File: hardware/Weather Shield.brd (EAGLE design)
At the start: 53.3 x 59.7 mm, 46 parts, among them Q1 BSS138, Q2 BSS138, U1 ARDUINO_R3_SHIELD, U2 3.3V MIC5219, U4 MPL3115A2LGA8, U5 HTU21D, U7 GP-635T, U8 TEMT6000

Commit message: Added power ctl to GPS and backup battery connection.
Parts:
- added JP1: Ext Batt, SparkFun-Connectors:1X01
- added LOGO1: OSHW-LOGOM, SparkFun-Aesthetics:OSHW-LOGO-M
- added R9: 1K, SparkFun:0603-RES
- moved FRAME1 63.6 mm to (-8.89, -24.1)
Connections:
- new net 3V_PWR_CTL: R9.2, U7.1
- net PWR_CTL: now also R9.1; no longer U7.1
- net V_BATT: now also JP1.1
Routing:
- net V_BATT: track 0.00 -> 12.2 mm, vias 0 -> 1
- net PWR_CTL: track 90.8 -> 79.8 mm
- net 3V_PWR_CTL: track 0.00 -> 9.31 mm
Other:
- board text added: "Ext Batt"
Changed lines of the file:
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@@
 <layer number="39" name="tKeepout" color="4" fill="11" visible="no" active="yes"/>
 <layer number="40" name="bKeepout" color="1" fill="11" visible="no" active="yes"/>
-<layer number="41" name="tRestrict" color="4" fill="10" visible="yes" active="yes"/>
-<layer number="42" name="bRestrict" color="1" fill="10" visible="yes" active="yes"/>
+<layer number="41" name="tRestrict" color="4" fill="10" visible="no" active="yes"/>
+<layer number="42" name="bRestrict" color="1" fill="10" visible="no" active="yes"/>
 <layer number="43" name="vRestrict" color="2" fill="10" visible="no" active="yes"/>
 <layer number="44" name="Drills" color="7" fill="1" visible="no" active="yes"/>
@@
 <wire x1="0" y1="57.15" x2="0" y2="2.54" width="0.2032" layer="20"/>
 <text x="17.907" y="1.27" size="1.524" layer="21" ratio="15">Weather Shield</text>
-<text x="-60.96" y="-33.02" size="1.778" layer="21" font="vector" ratio="15">N. Seidle</text>
+<text x="22.86" y="-24.13" size="1.778" layer="21" font="vector" ratio="15">N. Seidle</text>
 <text x="22.225" y="24.257" size="1.27" layer="21" ratio="15">Pressure</text>
 <text x="14.986" y="33.655" size="1.27" layer="21" ratio="15">Humidity</text>
@@
 <rectangle x1="13.97" y1="24.13" x2="40.64" y2="36.83" layer="41"/>
 <rectangle x1="13.97" y1="24.13" x2="40.64" y2="36.83" layer="42"/>
+<text x="32.004" y="13.462" size="1.27" layer="21" ratio="15">Ext Batt</text>
 </plain>
 <attributes>
@@
 <element name="C14" library="SparkFun-Passives" package="EIA3216" value="10uF" x="21.59" y="19.05" rot="R90"/>
 <element name="U1" library="SparkFun-Boards" package="UNO_R3_SHIELD" value="ARDUINO_R3_SHIELD" x="0" y="0"/>
-<element name="FRAME1" library="SparkFun-Aesthetics" package="CREATIVE_COMMONS" value="FRAME-LETTER" x="-72.39" y="-26.67"/>
+<element name="FRAME1" library="SparkFun-Aesthetics" package="CREATIVE_COMMONS" value="FRAME-LETTER" x="-8.89" y="-24.13"/>
 <element name="Q1" library="SparkFun" package="SOT23-3" value="BSS138" x="43.18" y="27.94"/>
 <element name="R3" library="SparkFun" package="0603-RES" value="4.7K" x="43.18" y="24.13"/>
@@
 <element name="R7" library="SparkFun" package="0603-RES" value="1K" x="40.64" y="20.32" rot="R90"/>
 <element name="R8" library="SparkFun" package="0603-RES" value="3.9K" x="38.1" y="20.32" rot="R270"/>
+<element name="LOGO1" library="SparkFun-Aesthetics" package="OSHW-LOGO-M" value="OSHW-LOGOM" x="26.67" y="43.18"/>
+<element name="R9" library="SparkFun" package="0603-RES" value="1K" x="41.91" y="11.43"/>
+<element name="JP1" library="SparkFun-Connectors" package="1X01" value="Ext Batt" x="41.91" y="13.97"/>
 </elements>
 <signals>
@@
 <signal name="V_BATT">
 <contactref element="U7" pad="2"/>
+<contactref element="JP1" pad="1"/>
+<wire x1="52.07" y1="10.43" x2="44.72" y2="10.43" width="0.254" layer="1"/>
+<wire x1="44.72" y1="10.43" x2="44.45" y2="10.414" width="0.254" layer="1"/>
+<via x="44.45" y="10.414" extent="1-16" drill="0.508"/>
+<wire x1="41.91" y1="13.97" x2="41.91" y2="12.954" width="0.254" layer="16"/>
+<wire x1="41.91" y1="12.954" x2="44.45" y2="10.414" width="0.254" layer="16"/>
 </signal>
 <signal name="LIGHT">
@@
 </signal>
 <signal name="PWR_CTL">
-<contactref element="U7" pad="1"/>
 <contactref element="U1" pad="D6"/>
-<wire x1="52.07" y1="11.43" x2="30.48" y2="11.43" width="0.254" layer="1"/>
 <wire x1="2.54" y1="39.37" x2="3.81" y2="39.37" width="0.254" layer="16"/>
 <wire x1="3.81" y1="39.37" x2="5.08" y2="38.1" width="0.254" layer="16"/>
@@
 <wire x1="17.78" y1="11.43" x2="30.48" y2="11.43" width="0.254" layer="16"/>
 <via x="30.48" y="11.43" extent="1-16" drill="0.508"/>
+<contactref element="R9" pad="1"/>
+<wire x1="41.06" y1="11.43" x2="30.48" y2="11.43" width="0.254" layer="1"/>
 </signal>
 <signal name="GTXO">
@@
 <wire x1="39.37" y1="19.47" x2="38.1" y2="19.47" width="0.254" layer="1"/>
 </signal>
+<signal name="3V_PWR_CTL">
+<contactref element="U7" pad="1"/>
+<contactref element="R9" pad="2"/>
+<wire x1="42.76" y1="11.43" x2="52.07" y2="11.43" width="0.254" layer="1"/>
+</signal>
 </signals>

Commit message: Tweaked schematic labels and connector for backup battery.
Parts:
- removed JP1: Ext Batt, SparkFun-Connectors:1X01
- added JP2: M02PTH, SparkFun-Connectors:1X02
- R9: value 1K -> 4.7K
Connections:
- net GND: now also JP2.1
- net V_BATT: now also JP2.2; no longer JP1.1
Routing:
- net V_BATT: track 12.2 -> 11.2 mm
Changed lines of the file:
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@@
 <element name="R8" library="SparkFun" package="0603-RES" value="3.9K" x="38.1" y="20.32" rot="R270"/>
 <element name="LOGO1" library="SparkFun-Aesthetics" package="OSHW-LOGO-M" value="OSHW-LOGOM" x="26.67" y="43.18"/>
-<element name="R9" library="SparkFun" package="0603-RES" value="1K" x="41.91" y="11.43"/>
-<element name="JP1" library="SparkFun-Connectors" package="1X01" value="Ext Batt" x="41.91" y="13.97"/>
+<element name="R9" library="SparkFun" package="0603-RES" value="4.7K" x="41.91" y="11.43"/>
+<element name="JP2" library="SparkFun-Connectors" package="1X02" value="M02PTH" x="44.45" y="13.97" rot="R180"/>
 </elements>
 <signals>
@@
 <wire x1="27.94" y1="25.4" x2="31.33" y2="25.4" width="0.254" layer="1"/>
 <wire x1="31.33" y1="26.67" x2="33.44" y2="26.67" width="0.254" layer="1"/>
+<contactref element="JP2" pad="1"/>
 </signal>
 <signal name="STAT2">
@@
 <signal name="V_BATT">
 <contactref element="U7" pad="2"/>
-<contactref element="JP1" pad="1"/>
 <wire x1="52.07" y1="10.43" x2="44.72" y2="10.43" width="0.254" layer="1"/>
 <wire x1="44.72" y1="10.43" x2="44.45" y2="10.414" width="0.254" layer="1"/>
 <via x="44.45" y="10.414" extent="1-16" drill="0.508"/>
-<wire x1="41.91" y1="13.97" x2="41.91" y2="12.954" width="0.254" layer="16"/>
 <wire x1="41.91" y1="12.954" x2="44.45" y2="10.414" width="0.254" layer="16"/>
+<contactref element="JP2" pad="2"/>
+<wire x1="41.91" y1="13.97" x2="41.91" y2="12.954" width="0" layer="19" extent="16-16"/>
 </signal>
 <signal name="LIGHT">

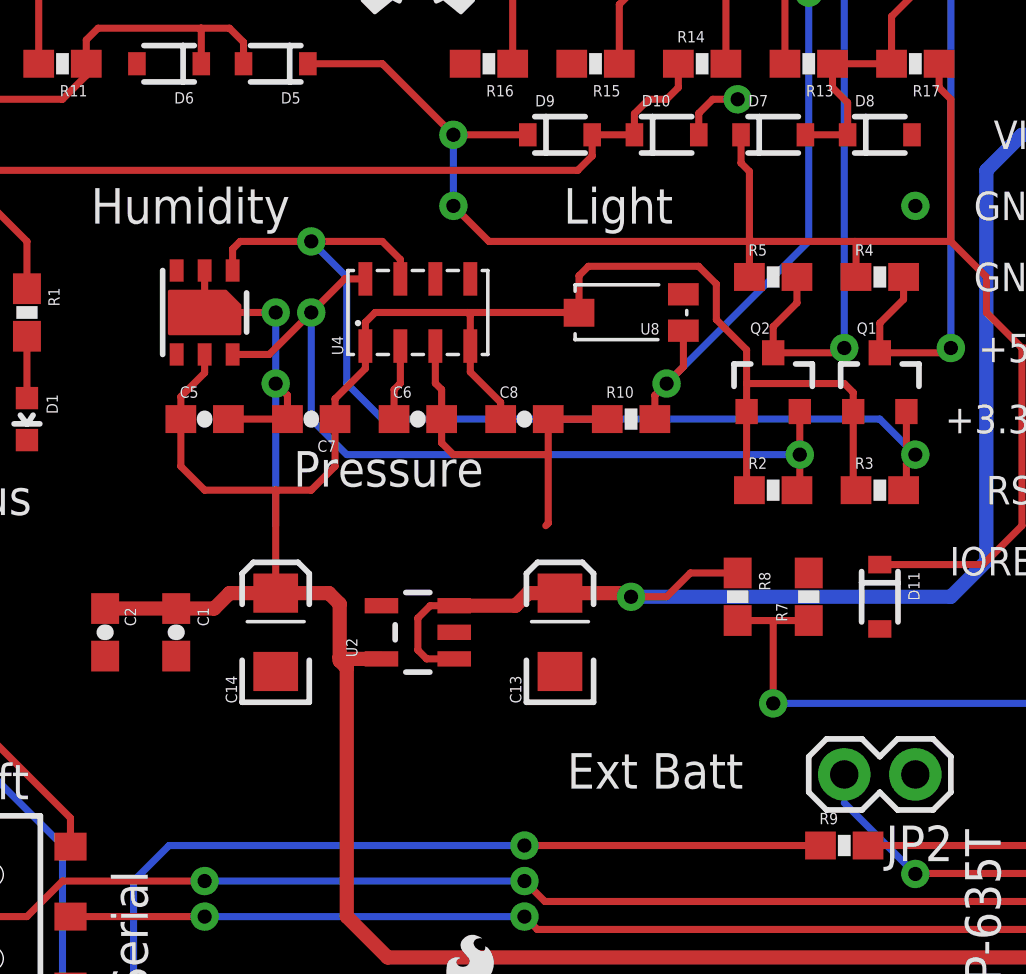
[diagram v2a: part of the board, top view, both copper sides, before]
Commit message: Added support for smaller, cheaper ALS-PT19 light sensor.
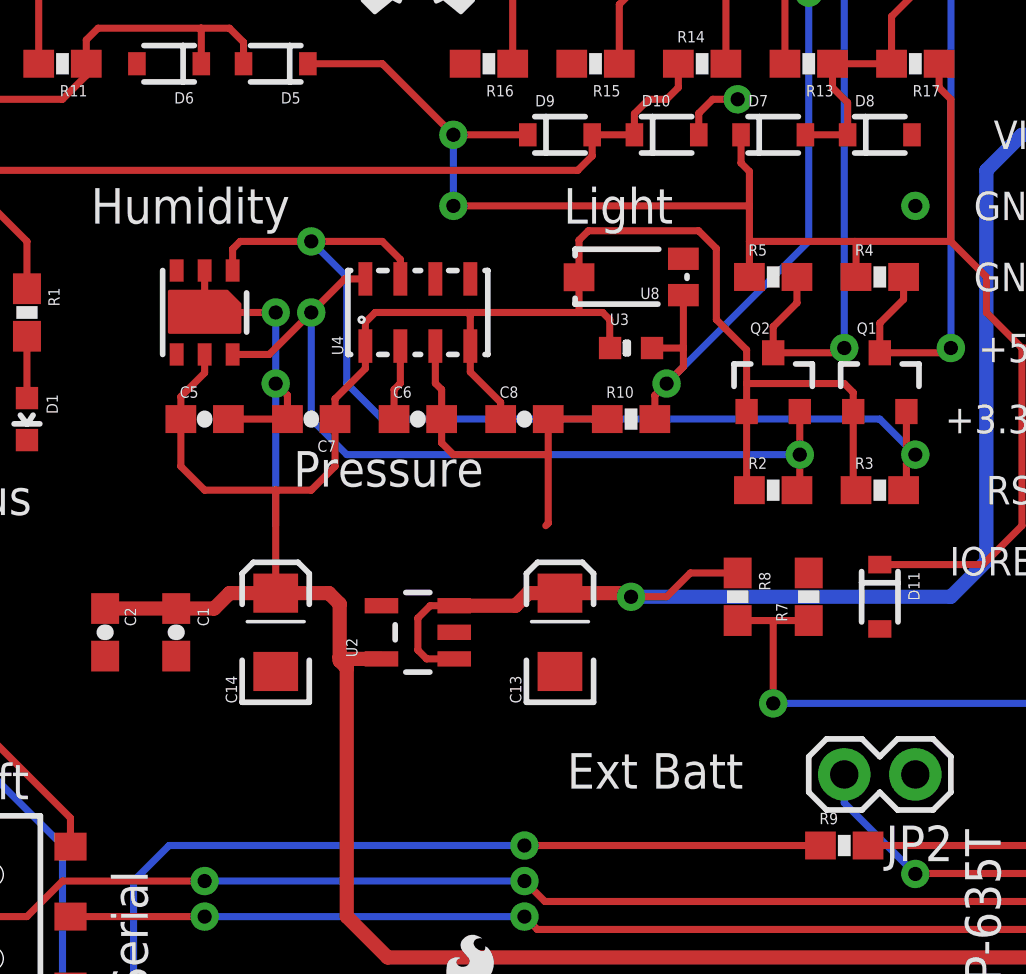
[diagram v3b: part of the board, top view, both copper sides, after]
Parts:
- added U3: ALS-PT19, SparkFun-Sensors:ALS-PT19
- moved U8 1.27 mm to (34.3, 31.8)
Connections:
- net 3.3V: now also U3.C
- net LIGHT: now also U3.E
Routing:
- net 3.3V: track 104.0 -> 108.8 mm
- net LIGHT: track 30.9 -> 33.3 mm
- net V_BATT: track 11.2 -> 12.2 mm
- net 5V: track 62.2 -> 61.7 mm
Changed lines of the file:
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@@
 <element name="U5" library="SparkFun-Sensors" package="HTU21D" value="HTU21D" x="19.05" y="30.48" rot="R90"/>
 <element name="U7" library="SparkFun-Connectors" package="JST-6-SMD-VERT-1.0MM" value="GP-635T" x="50.8" y="8.89" rot="R270"/>
-<element name="U8" library="SparkFun-Sensors" package="TEMT6000-SEN" value="TEMT6000" x="34.29" y="30.48" rot="R180"/>
+<element name="U8" library="SparkFun-Sensors" package="TEMT6000-SEN" value="TEMT6000" x="34.29" y="31.75" rot="R180"/>
 <element name="R10" library="SparkFun-Passives" package="0603-RES" value="10K" x="34.29" y="26.67"/>
 <element name="S2" library="SparkFun-Electromechanical" package="AYZ0202" value="Serial Select" x="11.43" y="8.89" rot="R90">
@@
 <element name="R9" library="SparkFun" package="0603-RES" value="4.7K" x="41.91" y="11.43"/>
 <element name="JP2" library="SparkFun-Connectors" package="1X02" value="M02PTH" x="44.45" y="13.97" rot="R180"/>
+<element name="U3" library="SparkFun-Sensors" package="ALS-PT19" value="ALS-PT19" x="34.29" y="29.21"/>
 </elements>
 <signals>
@@
 <wire x1="29.63" y1="27.266" x2="28.545" y2="28.351" width="0.254" layer="1"/>
 <wire x1="25.146" y1="30.48" x2="28.448" y2="30.48" width="0.254" layer="1"/>
-<wire x1="28.448" y1="30.48" x2="32.42" y2="30.48" width="0.254" layer="1"/>
-<wire x1="32.42" y1="30.48" x2="32.43" y2="30.47" width="0.254" layer="1"/>
+<wire x1="32.42" y1="31.75" x2="32.43" y2="31.74" width="0.254" layer="1"/>
 <wire x1="28.545" y1="29.28" x2="28.545" y2="30.383" width="0.254" layer="1"/>
 <wire x1="28.545" y1="30.383" x2="28.448" y2="30.48" width="0.254" layer="1"/>
-<wire x1="32.43" y1="30.47" x2="32.43" y2="31.795" width="0.254" layer="1"/>
-<wire x1="32.43" y1="31.795" x2="32.766" y2="32.131" width="0.254" layer="1"/>
-<wire x1="32.766" y1="32.131" x2="36.703" y2="32.131" width="0.254" layer="1"/>
-<wire x1="36.703" y1="32.131" x2="37.338" y2="31.496" width="0.254" layer="1"/>
-<wire x1="37.338" y1="31.496" x2="37.338" y2="30.226" width="0.254" layer="1"/>
+<wire x1="32.43" y1="31.74" x2="32.43" y2="33.065" width="0.254" layer="1"/>
+<wire x1="32.43" y1="33.065" x2="32.766" y2="33.401" width="0.254" layer="1"/>
+<wire x1="32.766" y1="33.401" x2="36.703" y2="33.401" width="0.254" layer="1"/>
+<wire x1="36.703" y1="33.401" x2="37.338" y2="32.766" width="0.254" layer="1"/>
 <wire x1="38.42" y1="26.94" x2="38.42" y2="27.94" width="0.254" layer="1"/>
 <wire x1="38.42" y1="27.94" x2="38.42" y2="29.144" width="0.254" layer="1"/>
-<wire x1="38.42" y1="29.144" x2="37.338" y2="30.226" width="0.254" layer="1"/>
+<contactref element="U3" pad="C"/>
+<wire x1="28.448" y1="30.48" x2="32.385" y2="30.48" width="0.254" layer="1"/>
+<wire x1="32.385" y1="30.48" x2="33.274" y2="30.48" width="0.254" layer="1"/>
+<wire x1="33.274" y1="30.48" x2="33.528" y2="30.226" width="0.254" layer="1"/>
+<wire x1="33.528" y1="30.226" x2="33.528" y2="29.222" width="0.254" layer="1"/>
+<wire x1="33.528" y1="29.222" x2="33.54" y2="29.21" width="0.254" layer="1"/>
+<wire x1="32.43" y1="31.74" x2="32.43" y2="30.525" width="0.254" layer="1"/>
+<wire x1="32.43" y1="30.525" x2="32.385" y2="30.48" width="0.254" layer="1"/>
+<wire x1="37.338" y1="32.766" x2="37.338" y2="30.226" width="0.254" layer="1"/>
+<wire x1="37.338" y1="30.226" x2="38.42" y2="29.144" width="0.254" layer="1"/>
 </signal>
 <signal name="SCL">
@@
 <wire x1="41.91" y1="12.954" x2="44.45" y2="10.414" width="0.254" layer="16"/>
 <contactref element="JP2" pad="2"/>
-<wire x1="41.91" y1="13.97" x2="41.91" y2="12.954" width="0" layer="19" extent="16-16"/>
+<wire x1="41.91" y1="12.954" x2="41.91" y2="13.97" width="0.254" layer="16"/>
 </signal>
 <signal name="LIGHT">
@@
 <wire x1="40.64" y1="33.02" x2="35.56" y2="27.94" width="0.254" layer="16"/>
 <via x="35.56" y="27.94" extent="1-16" drill="0.508"/>
-<wire x1="36.16" y1="29.83" x2="36.16" y2="28.54" width="0.254" layer="1"/>
+<wire x1="36.16" y1="31.1" x2="36.16" y2="29.21" width="0.254" layer="1"/>
+<wire x1="36.16" y1="29.21" x2="36.16" y2="28.54" width="0.254" layer="1"/>
 <wire x1="36.16" y1="28.54" x2="35.56" y2="27.94" width="0.254" layer="1"/>
 <wire x1="35.14" y1="26.67" x2="35.14" y2="27.52" width="0.254" layer="1"/>
 <wire x1="35.14" y1="27.52" x2="35.56" y2="27.94" width="0.254" layer="1"/>
+<contactref element="U3" pad="E"/>
+<wire x1="35.04" y1="29.21" x2="36.16" y2="29.21" width="0.254" layer="1"/>
 </signal>
 <signal name="PWR_CTL">
@@
 <wire x1="46.99" y1="31.75" x2="45.72" y2="33.02" width="0.254" layer="1"/>
 <wire x1="45.72" y1="33.02" x2="42.291" y2="33.02" width="0.254" layer="1"/>
-<wire x1="42.291" y1="33.02" x2="38.608" y2="33.02" width="0.254" layer="1"/>
-<wire x1="38.608" y1="33.02" x2="38.52" y2="33.02" width="0.254" layer="1"/>
+<wire x1="42.291" y1="33.02" x2="38.52" y2="33.02" width="0.254" layer="1"/>
 <wire x1="42.33" y1="32.981" x2="42.291" y2="33.02" width="0.254" layer="1"/>
 <wire x1="45.3" y1="39.37" x2="45.3" y2="38.52" width="0.254" layer="1"/>
 <wire x1="45.3" y1="38.52" x2="45.72" y2="38.1" width="0.254" layer="1"/>
 <wire x1="45.72" y1="38.1" x2="45.72" y2="33.02" width="0.254" layer="1"/>
-<wire x1="38.52" y1="33.02" x2="29.21" y2="33.02" width="0.254" layer="1"/>
-<wire x1="29.21" y1="33.02" x2="27.94" y2="34.29" width="0.254" layer="1"/>
 <via x="27.94" y="34.29" extent="1-16" drill="0.508"/>
 <wire x1="27.94" y1="34.29" x2="27.94" y2="36.83" width="0.254" layer="16"/>
 <via x="27.94" y="36.83" extent="1-16" drill="0.508"/>
-<wire x1="38.52" y1="35.521" x2="38.52" y2="33.108" width="0.254" layer="1"/>
-<wire x1="38.52" y1="33.108" x2="38.608" y2="33.02" width="0.254" layer="1"/>
+<wire x1="38.52" y1="35.521" x2="38.52" y2="34.29" width="0.254" layer="1"/>
 <wire x1="43.18" y1="21.47" x2="46.87" y2="21.47" width="0.254" layer="1"/>
 <wire x1="46.87" y1="21.47" x2="48.26" y2="22.86" width="0.254" layer="1"/>
 <wire x1="48.26" y1="22.86" x2="48.26" y2="29.21" width="0.254" layer="1"/>
+<wire x1="27.94" y1="34.29" x2="38.52" y2="34.29" width="0.254" layer="1"/>
+<wire x1="38.52" y1="33.02" x2="38.52" y2="34.29" width="0.254" layer="1"/>
 </signal>
 <signal name="RAIN">
